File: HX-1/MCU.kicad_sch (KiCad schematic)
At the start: 38 parts, among them J10 Conn_01x20, J11 Conn_01x20, J12 USART_CONN, J3 I2C_CONN, J4 SPI_CONN, J7 FDCAN_CONN, J8 UART_CONN, SW1 SW_SPDT, U1 STM32H723ZGT6

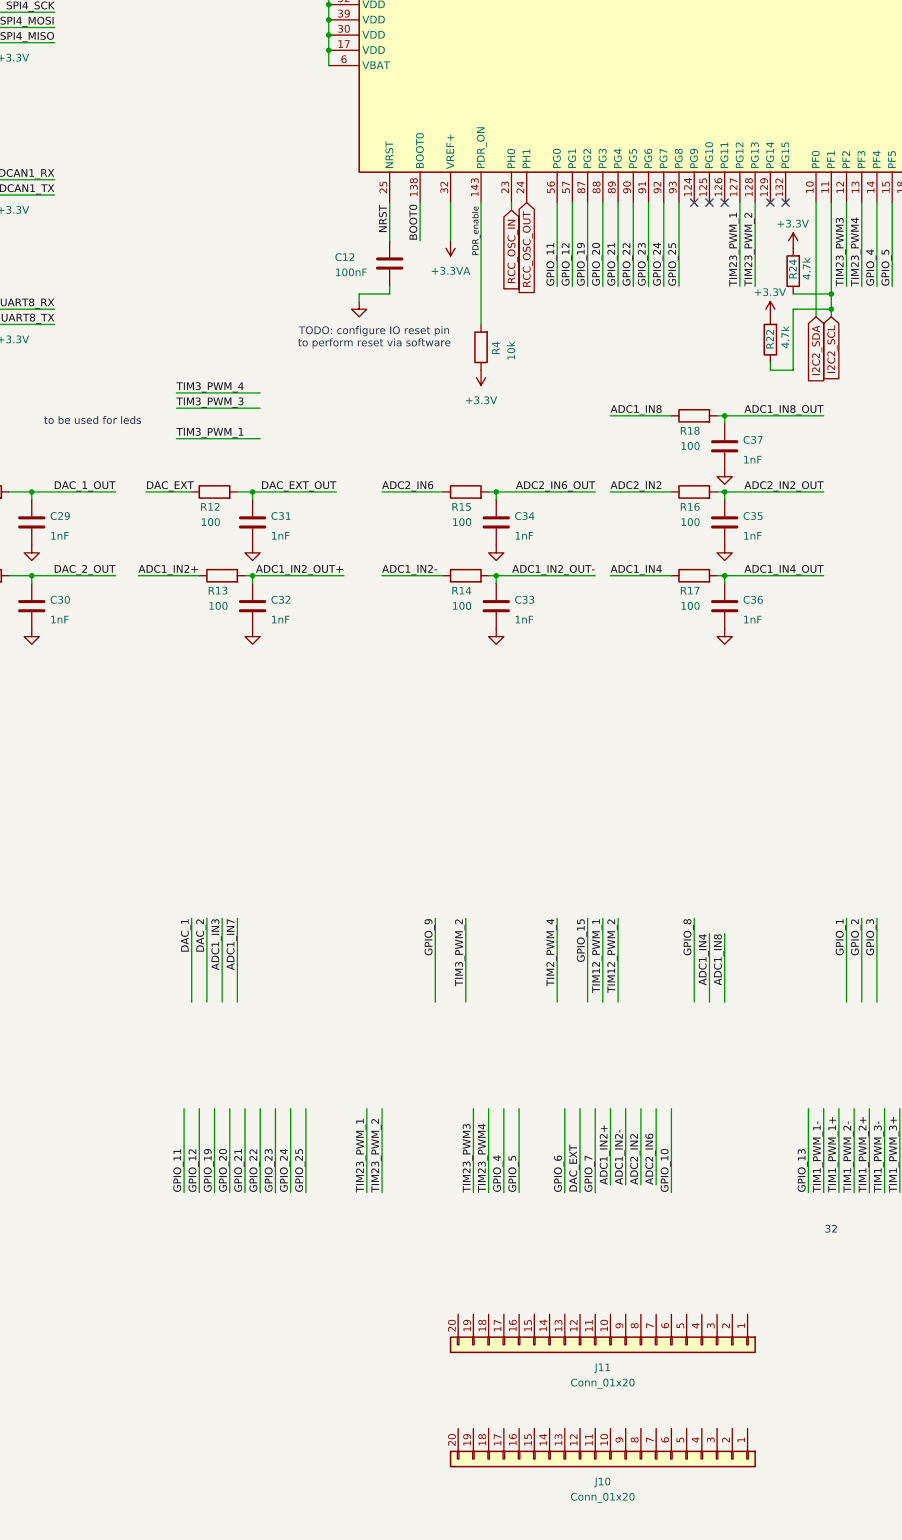
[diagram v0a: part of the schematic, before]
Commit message: add 3v3 led and pwm led, position mounting holes and pin header
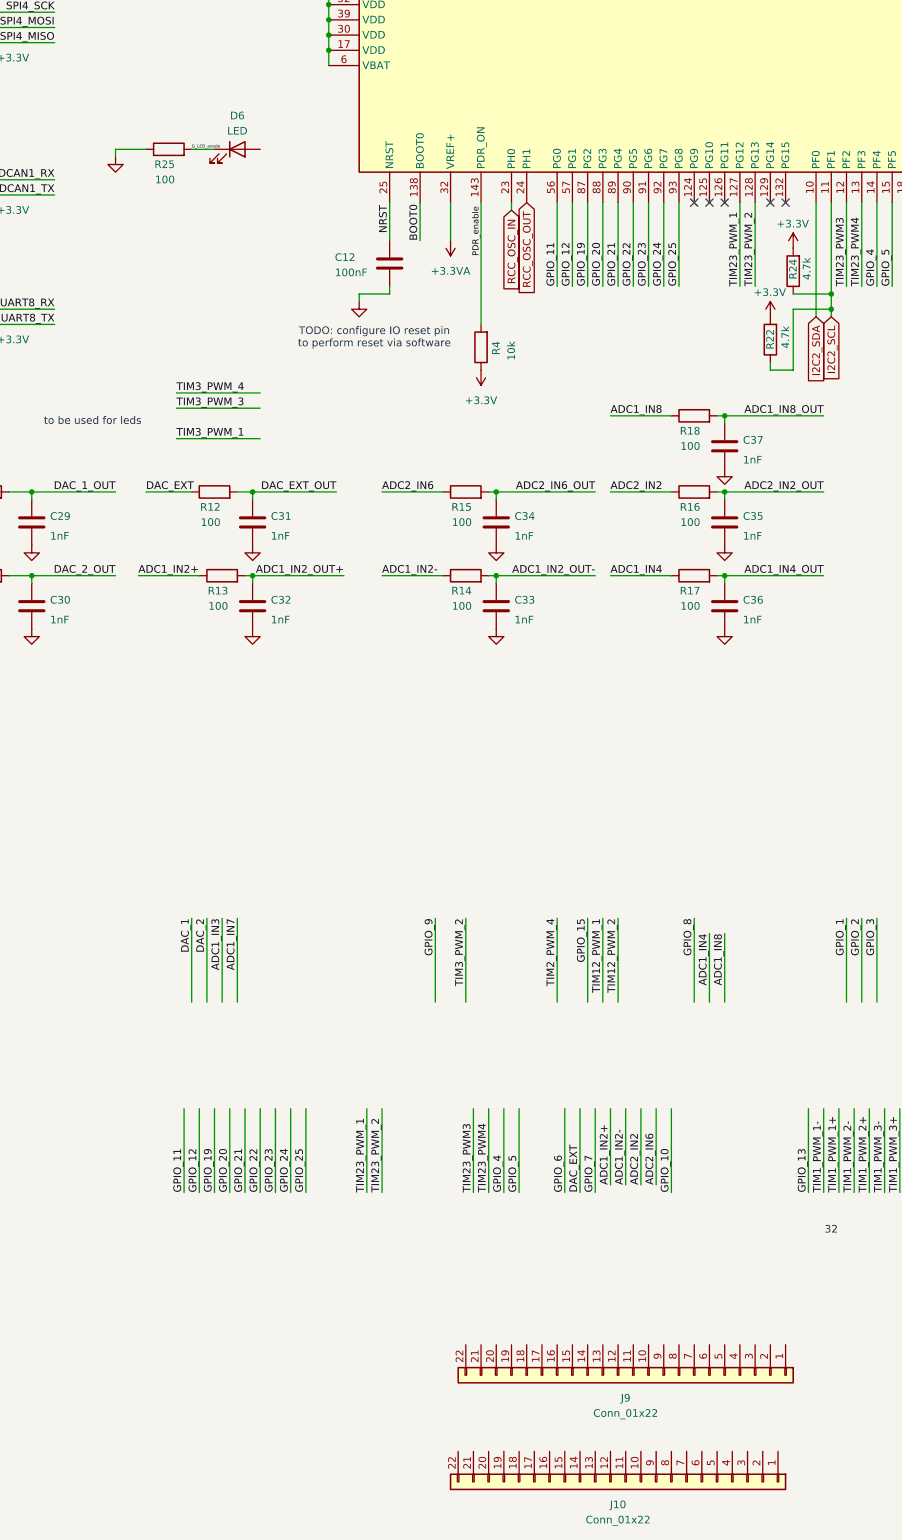
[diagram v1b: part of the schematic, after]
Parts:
- removed J10, J11: Conn_01x20, Connector_PinHeader_2.54mm:PinHeader_1x20_P2.54mm_Vertical, symbol Connector_Generic:Conn_01x20
- added D6: LED, LED_SMD:LED_0805_2012Metric, symbol Device:LED
- added J10, J9: Conn_01x22, Connector_PinHeader_2.54mm:PinHeader_1x24_P2.54mm_Vertical, symbol Connector_Generic:Conn_01x22
- added R25: 100, Resistor_SMD:R_0402_1005Metric, symbol Device:R
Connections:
- net GND: now also R25.1
- new net G_LED_anode: D6.1 (K), R25.2

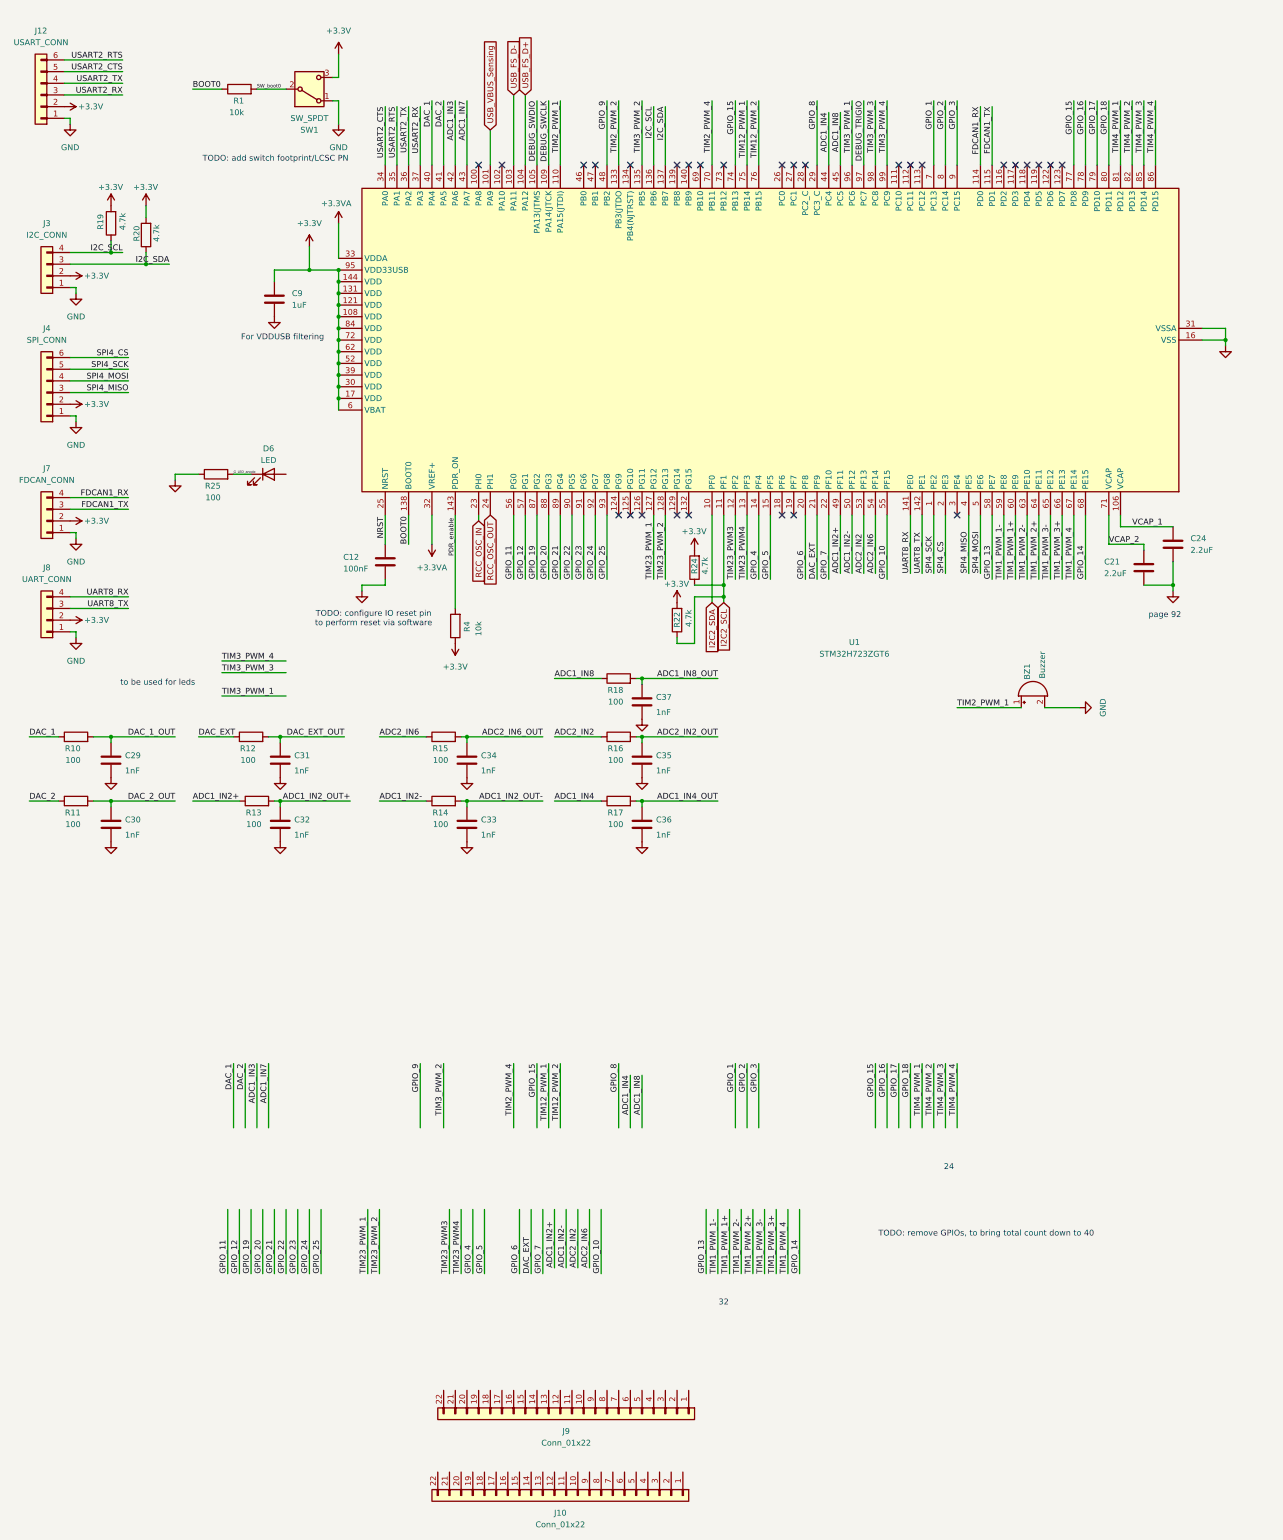
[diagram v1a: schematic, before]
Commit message: map out traces for all I/Os, remove some ADC, PWM and GPIO for space
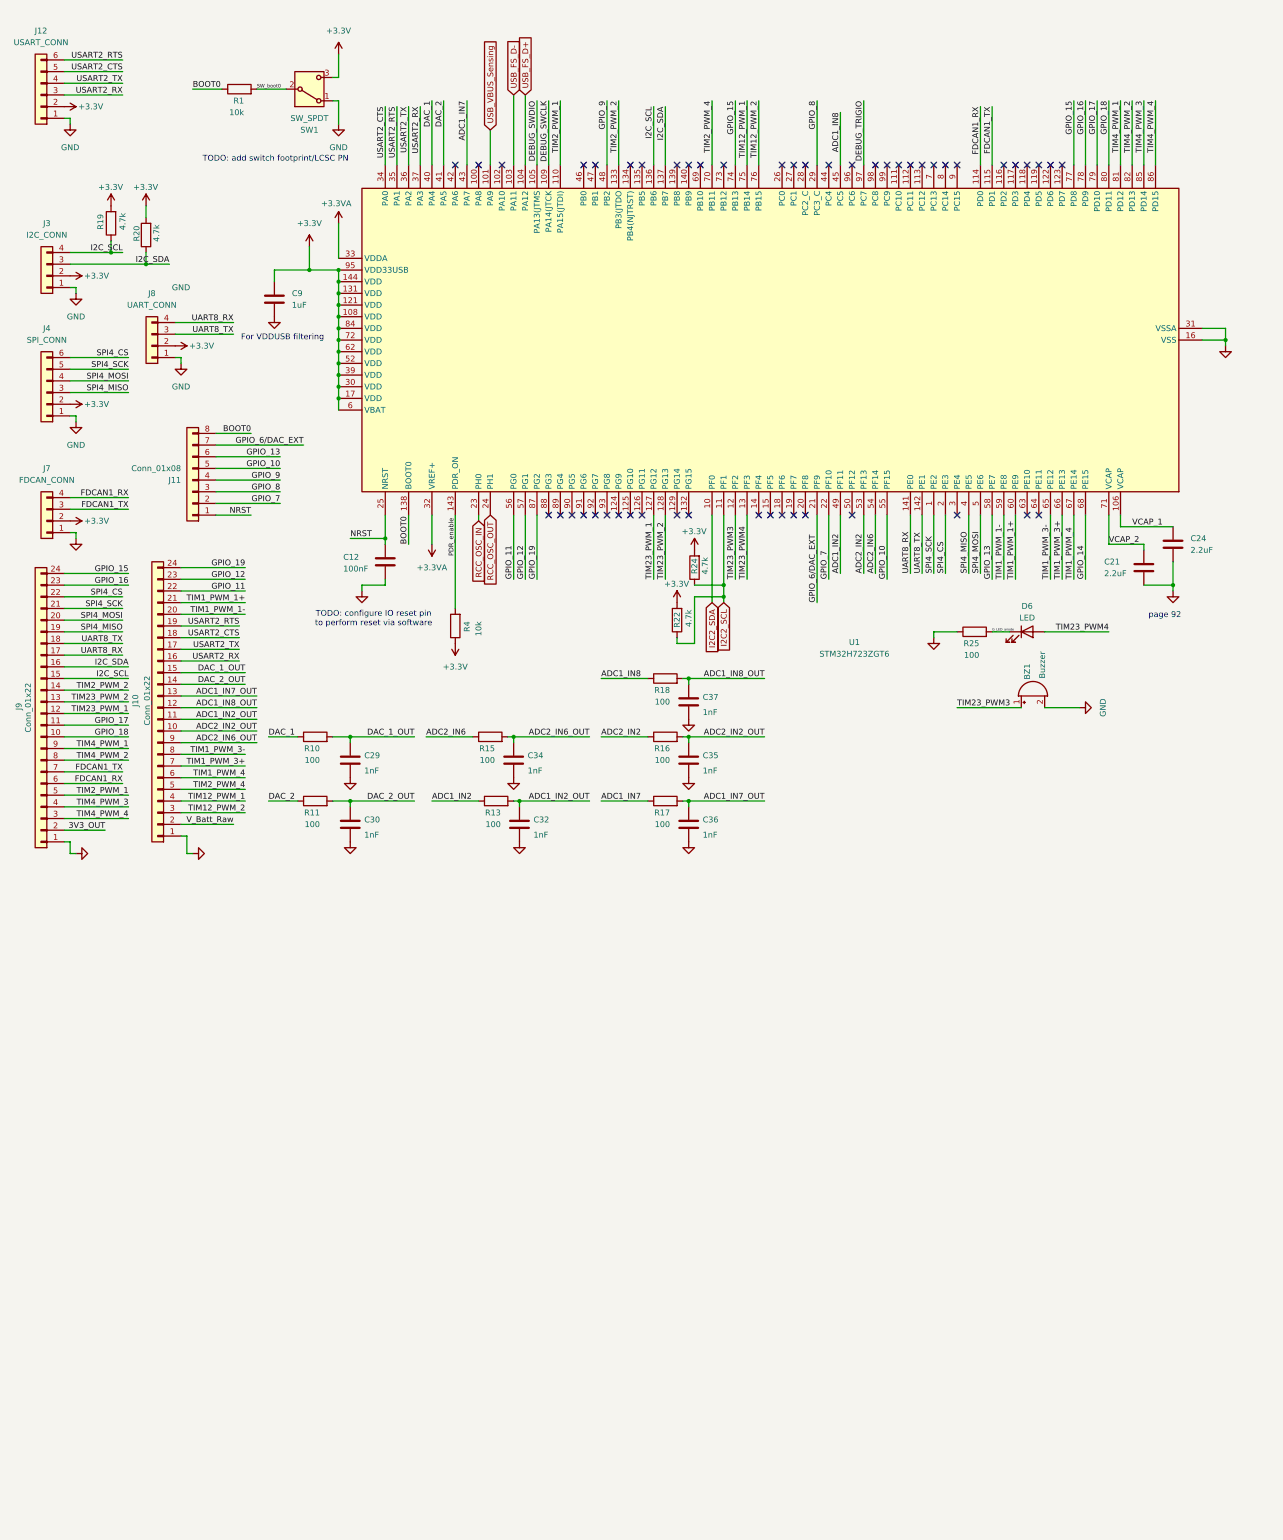
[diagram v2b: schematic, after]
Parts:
- removed C31, C33: 1nF, Capacitor_SMD:C_0603_1608Metric, symbol Device:C
- removed R12, R14: 100, Resistor_SMD:R_0402_1005Metric, symbol Device:R
- added J11: Conn_01x08, Connector_PinHeader_2.54mm:PinHeader_1x08_P2.54mm_Vertical, symbol Connector_Generic:Conn_01x08
- J10, J9: symbol Connector_Generic:Conn_01x22 -> Connector_Generic:Conn_01x24; now in the parts list
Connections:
- net ADC1_IN2_OUT+ is gone; now on net ADC1_IN2_OUT: C32.1, R13.2
- net ADC1_IN4_OUT is gone; now on net ADC1_IN7_OUT: C36.1, R17.2
- net ADC1_IN7: now also R17.1
- net ADC1_IN8_OUT: now also J10.12 (Pin_12)
- net ADC2_IN2_OUT: now also J10.10 (Pin_10)
- net ADC2_IN6_OUT: now also J10.9 (Pin_9)
- net BOOT0: now also J11.8 (Pin_8)
- net DAC_1_OUT: now also J10.15 (Pin_15)
- net DAC_2_OUT: now also J10.14 (Pin_14)
- net FDCAN1_RX: now also J9.6 (Pin_6)
- net FDCAN1_TX: now also J9.7 (Pin_7)
- net GND: now also J10.1 (Pin_1), J9.1 (Pin_1)
- net GPIO_10: now also J11.5 (Pin_5)
- net GPIO_11: now also J10.22 (Pin_22)
- net GPIO_12: now also J10.23 (Pin_23)
- net GPIO_13: now also J11.6 (Pin_6)
- net GPIO_15: now also J9.24 (Pin_24)
- net GPIO_16: now also J9.23 (Pin_23)
- net GPIO_17: now also J9.11 (Pin_11)
- net GPIO_18: now also J9.10 (Pin_10)
- net GPIO_19: now also J10.24 (Pin_24)
- net GPIO_7: now also J11.2 (Pin_2)
- net GPIO_8: now also J11.3 (Pin_3)
- net GPIO_9: now also J11.4 (Pin_4)
- net I2C_SCL: now also J9.15 (Pin_15)
- net I2C_SDA: now also J9.16 (Pin_16)
- net NRST: now also J11.1 (Pin_1)
- net SPI4_CS: now also J9.22 (Pin_22)
- net SPI4_MISO: now also J9.19 (Pin_19)
- net SPI4_MOSI: now also J9.20 (Pin_20)
- net SPI4_SCK: now also J9.21 (Pin_21)
- net TIM12_PWM_1: now also J10.4 (Pin_4)
- net TIM12_PWM_2: now also J10.3 (Pin_3)
- net TIM1_PWM_1+: now also J10.21 (Pin_21)
- net TIM1_PWM_1-: now also J10.20 (Pin_20)
- net TIM1_PWM_3+: now also J10.7 (Pin_7)
- net TIM1_PWM_3-: now also J10.8 (Pin_8)
- net TIM1_PWM_4: now also J10.6 (Pin_6)
- net TIM23_PWM3: now also BZ1.1 (-)
- net TIM23_PWM4: now also D6.2 (A)
- net TIM23_PWM_1: now also J9.12 (Pin_12)
- net TIM23_PWM_2: now also J9.13 (Pin_13)
- net TIM2_PWM_1: now also J9.5 (Pin_5); no longer BZ1.1 (-)
- net TIM2_PWM_2: now also J9.14 (Pin_14)
- net TIM2_PWM_4: now also J10.5 (Pin_5)
- net TIM4_PWM_1: now also J9.9 (Pin_9)
- net TIM4_PWM_2: now also J9.8 (Pin_8)
- net TIM4_PWM_3: now also J9.4 (Pin_4)
- net TIM4_PWM_4: now also J9.3 (Pin_3)
- net UART8_RX: now also J9.17 (Pin_17)
- net UART8_TX: now also J9.18 (Pin_18)
- net USART2_CTS: now also J10.18 (Pin_18)
- net USART2_RTS: now also J10.19 (Pin_19)
- net USART2_RX: now also J10.16 (Pin_16)
- net USART2_TX: now also J10.17 (Pin_17)
- net ADC1_IN2_OUT: now reaches J10.11 (Pin_11)
- net ADC1_IN7_OUT: now reaches J10.13 (Pin_13)
- net V_Batt_Raw: now reaches J10.2 (Pin_2)
- net 3V3_OUT: now reaches J9.2 (Pin_2)
- net ADC1_IN2+ renamed ADC1_IN2
- net ADC1_IN2-: no longer names the net of U1.50 (PF12)
- net ADC1_IN3: no longer names the net of U1.42 (PA6)
- net ADC1_IN4: no longer names the net of U1.44 (PC4)
- net ADC1_IN4: no longer R17.1
- net DAC_EXT renamed GPIO_6/DAC_EXT
- net GPIO_6/DAC_EXT: now also J11.7 (Pin_7)
- net GPIO_1: no longer names the net of U1.7 (PC13)
- net GPIO_2: no longer names the net of U1.8 (PC14)
- net GPIO_20: no longer names the net of U1.88 (PG3)
- net GPIO_21: no longer names the net of U1.89 (PG4)
- net GPIO_22: no longer names the net of U1.90 (PG5)
- net GPIO_23: no longer names the net of U1.91 (PG6)
- net GPIO_24: no longer names the net of U1.92 (PG7)
- net GPIO_25: no longer names the net of U1.93 (PG8)
- net GPIO_3: no longer names the net of U1.9 (PC15)
- net GPIO_4: no longer names the net of U1.14 (PF4)
- net GPIO_5: no longer names the net of U1.15 (PF5)
- net GPIO_6: no longer names the net of U1.20 (PF8)
- net TIM1_PWM_2+: no longer names the net of U1.64 (PE11)
- net TIM1_PWM_2-: no longer names the net of U1.63 (PE10)
- net TIM3_PWM_1: no longer names the net of U1.96 (PC6)
- net TIM3_PWM_2: no longer names the net of U1.135 (PB5)
- net TIM3_PWM_3: no longer names the net of U1.98 (PC8)
- net TIM3_PWM_4: no longer names the net of U1.99 (PC9)
- no-connect marks 29 -> 50
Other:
- note removed: "24"
- note removed: "32"
- note removed: "TODO: remove GPIOs, to bring total count down to 40"
- note removed: "to be used for leds"
- moved on the sheet: C29, C30, C32, C34, C35, C36, C37, D6, J8, R10, R11, R13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
